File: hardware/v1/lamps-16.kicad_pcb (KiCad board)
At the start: 2 copper layers, 198.1 x 25.4 mm, 17 parts, among them P10 CONN_02X05

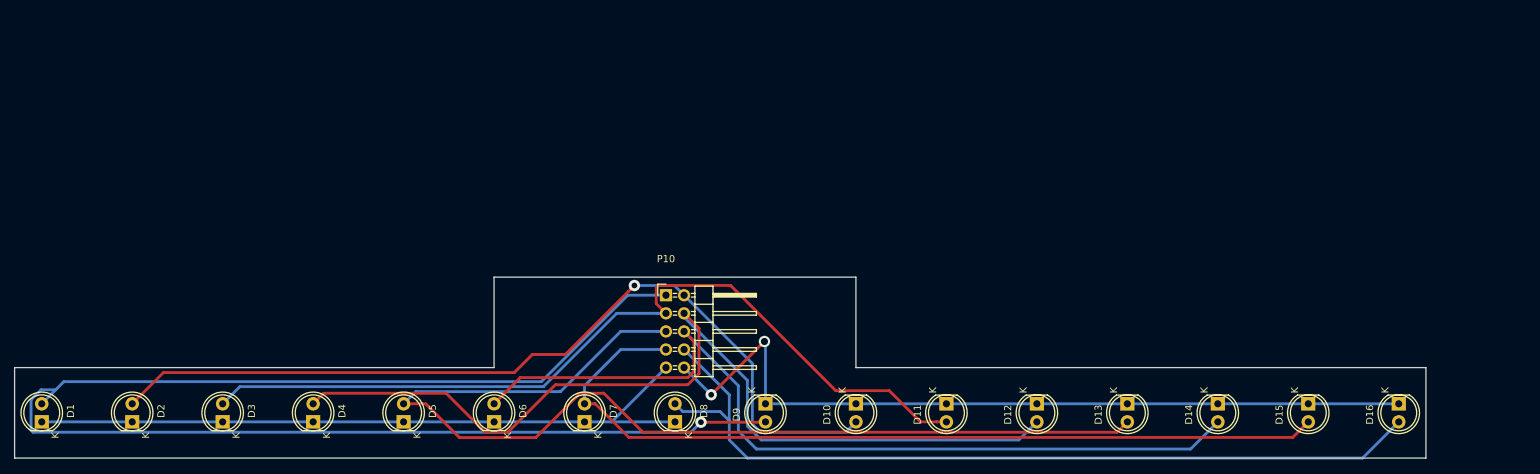
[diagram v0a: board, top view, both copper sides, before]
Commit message: More routing experiments.
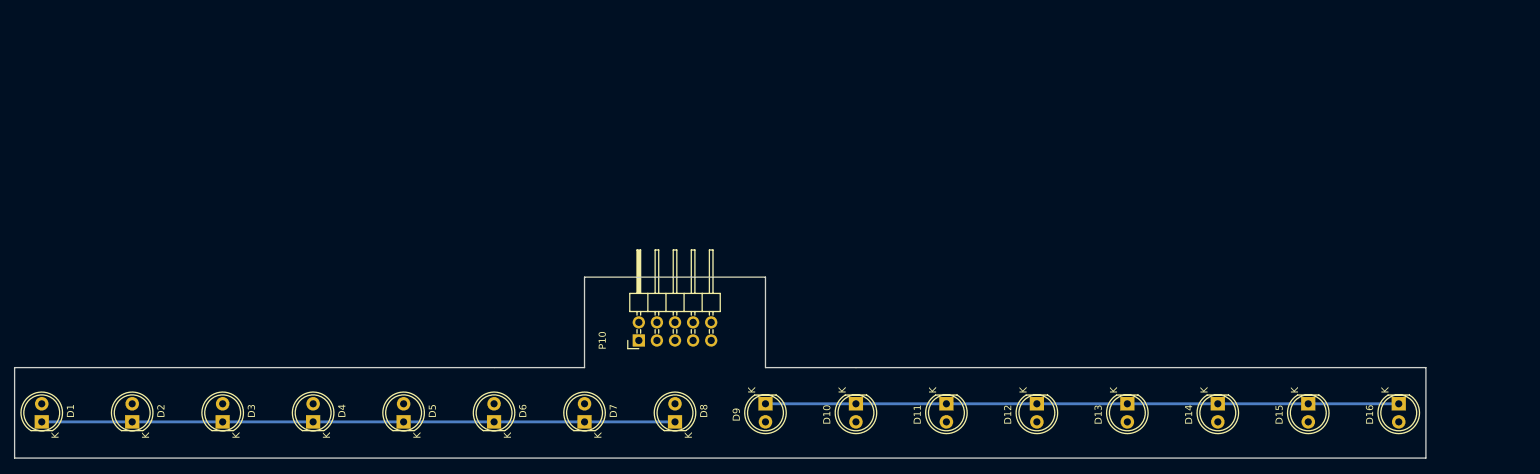
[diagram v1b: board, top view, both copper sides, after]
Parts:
- moved P10 7.41 mm to (109.2, 110.5), turned to 90 degrees
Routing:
- net /SEG0: track 206.1 -> 0.00 mm, vias 1 -> 0
- net /SEG4: track 150.1 -> 0.00 mm
- net /SEG3: track 131.8 -> 0.00 mm
- net /SEG5: track 123.2 -> 0.00 mm
- net /SEG1: track 122.6 -> 0.00 mm, vias 1 -> 0
- net /SEG7: track 121.1 -> 0.00 mm
- net /SEG6: track 120.5 -> 0.00 mm
- net /SEG2: track 120.5 -> 0.00 mm
- net /DIGITB: track 113.7 -> 88.9 mm, vias 2 -> 0
- net /DIGITA: track 99.7 -> 88.9 mm
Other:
- outline, holes or cut-outs redrawn

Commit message: Manually route lmaps-16 board
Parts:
- moved P10 67.1 mm to (50.8, 77.5)
- moved D1 35.4 mm to (38.1, 88.9)
- moved D3 35.4 mm to (63.5, 88.9)
- moved D4 35.4 mm to (76.2, 88.9)
- moved D5 35.4 mm to (88.9, 88.9)
- moved D7 35.4 mm to (114.3, 88.9)
- moved D8 35.4 mm to (127.0, 88.9)
- moved D2 35.4 mm to (50.8, 88.9)
- moved D6 35.4 mm to (101.6, 88.9)
- moved D10 33.0 mm to (152.4, 88.9), turned to 90 degrees
- moved D12 33.0 mm to (177.8, 88.9), turned to 90 degrees
- moved D15 33.0 mm to (215.9, 88.9), turned to 90 degrees
- moved D11 33.0 mm to (165.1, 88.9), turned to 90 degrees
- moved D13 33.0 mm to (190.5, 88.9), turned to 90 degrees
- moved D14 33.0 mm to (203.2, 88.9), turned to 90 degrees
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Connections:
- P10 pad 1: /SEG0 -> /SEG1
- P10 pad 10: /DIGITB -> /SEG6
- P10 pad 2: /SEG1 -> /SEG0
- P10 pad 4: /SEG3 -> /DIGITA
- P10 pad 5: /SEG4 -> /SEG3
- P10 pad 6: /SEG5 -> /DIGITB
- P10 pad 7: /SEG6 -> /SEG4
- P10 pad 9: /DIGITA -> /SEG5
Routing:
- net /DIGITB: track 88.9 -> 273.5 mm
- net /SEG7: track 0.00 -> 183.4 mm, vias 0 -> 1
- net /SEG6: track 0.00 -> 166.0 mm, vias 0 -> 1
- net /SEG5: track 0.00 -> 151.6 mm, vias 0 -> 1
- net /SEG4: track 0.00 -> 140.7 mm, vias 0 -> 1
- net /SEG3: track 0.00 -> 130.3 mm, vias 0 -> 1
- net /SEG2: track 0.00 -> 119.3 mm, vias 0 -> 1
- net /SEG0: track 0.00 -> 117.4 mm
- net /SEG1: track 0.00 -> 111.8 mm, vias 0 -> 1
- net /DIGITA: track 88.9 -> 123.2 mm
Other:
- board size 198.1 x 25.4 mm -> 198.1 x 20.3 mm

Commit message: Add m3 holes and re-route around them for led boards.
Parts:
- added REF**: M3, myparts:HOLE_M3, F.Cu at (44.5, 82.5)
- added REF**: M3, myparts:HOLE_M3, F.Cu at (222.2, 82.5)
- D1, D10, D11, D12, D13, D14, D15, D16, D2, D3, D4, D5, D6, D7, D8, D9: footprint LEDs:LED-5MM -> myparts:LED-5MM-custom
- moved P1 3.81 mm to (47.0, 77.5)
- renumbered P10 to P1
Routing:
- net /DIGITA: track 123.2 -> 115.1 mm
- net /DIGITB: track 273.5 -> 279.7 mm
- net /SEG7: track 183.4 -> 188.7 mm
- net /SEG5: track 151.6 -> 155.4 mm
- net /SEG4: track 140.7 -> 144.6 mm
- net /SEG6: track 166.0 -> 169.7 mm
- net /SEG2: track 119.3 -> 122.7 mm
- net /SEG3: track 130.3 -> 133.6 mm
- net /SEG1: track 111.8 -> 113.4 mm
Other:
- board size 198.1 x 20.3 mm -> 198.1 x 19.7 mm
